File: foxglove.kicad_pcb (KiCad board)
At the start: 4 copper layers, 82.8 x 53.3 mm, 177 parts, among them IC1 LFE5U-12F-6BG256C, J1 NEIGHBOR1, J2 NEIGHBOR2, J3 Conn_02x05_Odd_Even, J4 Conn_02x10_Odd_Even, J5 Conn_01x02_Female, J6 Conn_02x03_Odd_Even, J7 BONUS_ROW, U1 LM393, U10 SHIFTER, U11 74HC4051, U12 SHIFTER, U13 74HC4051, U14 SHIFTER, U15 74HC4051, U16 SHIFTER, U17 74HC4051, U18 SHIFTER, U19 74HC4051, U2 ADP225, U20 SHIFTER, U21 74HC4051, U22 SHIFTER, U23 74HC4051, U24 SHIFTER, U25 74LVC1G53, U26 PCA6408A, U3 AP2127, U4 74LVC1G3157, U5 AP2127, U6 AP2127, U7 DAC084S085, U8 AT25xxx, U9 74HC4051

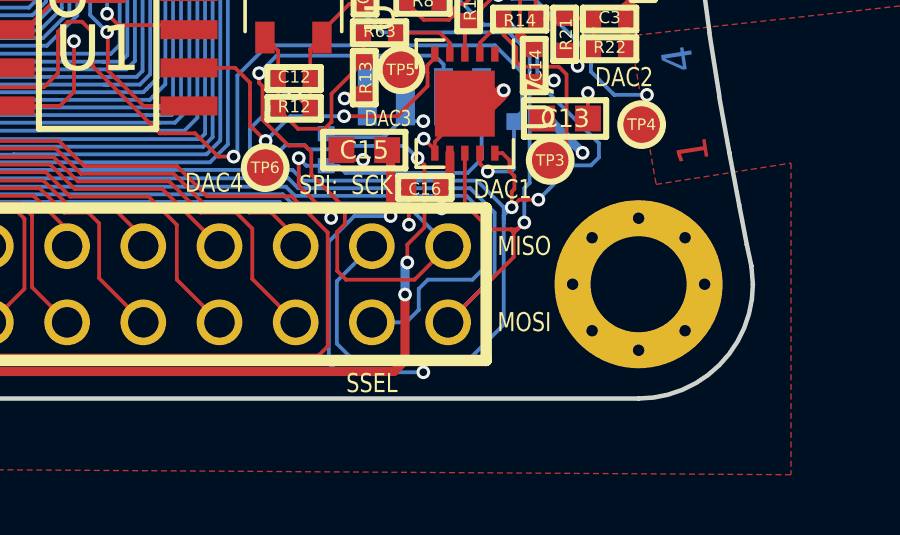
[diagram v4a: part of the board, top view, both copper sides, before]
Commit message: adopt OSHWA convention for SPI signal names https://www.oshwa.org/a-resolution-to-redefine-spi-signal-names
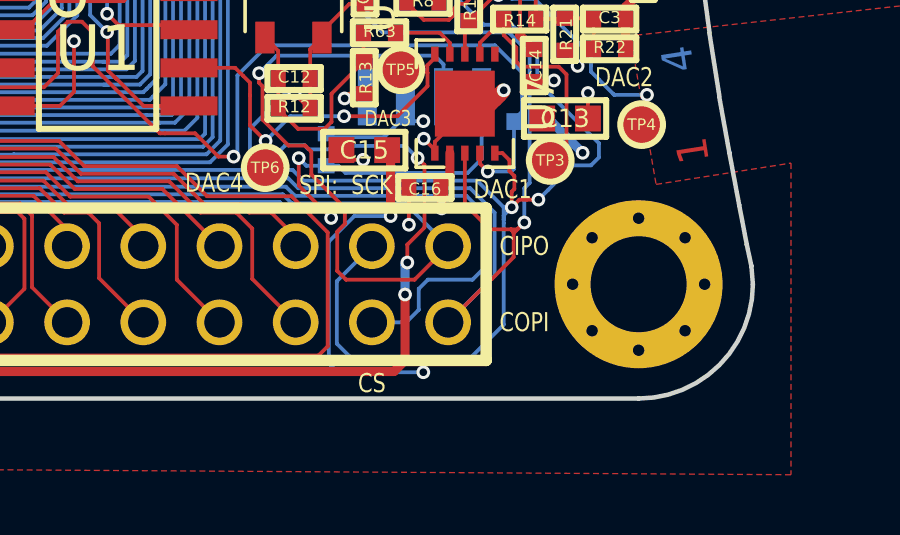
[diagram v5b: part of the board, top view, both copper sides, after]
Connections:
- net /MISO renamed /CIPO
- net /MOSI renamed /COPI
- net /SSEL renamed /CS
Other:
- board text added: "CIPO"
- board text added: "COPI"
- board text added: "CS"
- board text removed: "MISO"
- board text removed: "MOSI"
- board text removed: "SSEL"
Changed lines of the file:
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@@
   (net 18 /J1.35)
   (net 19 /J1.36)
-  (net 20 /SSEL)
+  (net 20 /CS)
   (net 21 /SCK)
-  (net 22 /MOSI)
-  (net 23 /MISO)
+  (net 22 /COPI)
+  (net 23 /CIPO)
   (net 24 /ADC)
   (net 25 /J2.09)
@@
     (add_net /J7.17)
     (add_net /J7.18)
-    (add_net /MISO)
-    (add_net /MOSI)
+    (add_net /CIPO)
+    (add_net /COPI)
     (add_net /PROGRAMN)
     (add_net /S0_1)
@@
     (add_net /S2_8)
     (add_net /SCK)
-    (add_net /SSEL)
+    (add_net /CS)
     (add_net /TCK)
     (add_net /TDI)
@@
       (net 94 /INITN))
     (pad T8 smd circle (at -0.4 6 90) (size 0.41 0.41) (layers F.Cu F.Paste F.Mask)
-      (net 22 /MOSI))
+      (net 22 /COPI))
     (pad T7 smd circle (at -1.2 6 90) (size 0.41 0.41) (layers F.Cu F.Paste F.Mask)
-      (net 23 /MISO))
+      (net 23 /CIPO))
     (pad T6 smd circle (at -2 6 90) (size 0.41 0.41) (layers F.Cu F.Paste F.Mask)
       (net 101 /J1.22))
@@
       (net 91 /PROGRAMN))
     (pad R8 smd circle (at -0.4 5.2 90) (size 0.41 0.41) (layers F.Cu F.Paste F.Mask)
-      (net 20 /SSEL))
+      (net 20 /CS))
     (pad R7 smd circle (at -1.2 5.2 90) (size 0.41 0.41) (layers F.Cu F.Paste F.Mask)
       (net 241 "Net-(IC1-PadR7)"))
@@
     (fp_line (start -25.4 -2.54) (end 25.4 -2.54) (layer F.SilkS) (width 0.381))
     (pad 40 thru_hole circle (at 24.13 -1.27) (size 1.524 1.524) (drill 1.016) (layers *.Cu *.Mask F.SilkS)
-      (net 23 /MISO))
+      (net 23 /CIPO))
     (pad 39 thru_hole circle (at 24.13 1.27) (size 1.524 1.524) (drill 1.016) (layers *.Cu *.Mask F.SilkS)
-      (net 22 /MOSI))
+      (net 22 /COPI))
     (pad 38 thru_hole circle (at 21.59 -1.27) (size 1.524 1.524) (drill 1.016) (layers *.Cu *.Mask F.SilkS)
       (net 21 /SCK))
     (pad 37 thru_hole circle (at 21.59 1.27) (size 1.524 1.524) (drill 1.016) (layers *.Cu *.Mask F.SilkS)
-      (net 20 /SSEL))
+      (net 20 /CS))
     (pad 36 thru_hole circle (at 19.05 -1.27) (size 1.524 1.524) (drill 1.016) (layers *.Cu *.Mask F.SilkS)
       (net 19 /J1.36))
@@
       (net 292 /DAC~SYNC~))
     (pad 8 smd rect (at 1.65 0 270) (size 0.5 0.25) (layers F.Cu F.Paste F.Mask)
-      (net 22 /MOSI))
+      (net 22 /COPI))
     (pad 5 smd rect (at -1.65 1 270) (size 0.5 0.25) (layers F.Cu F.Paste F.Mask)
       (net 65 /DAC4))
@@
       (net 88 /CSSPIN))
     (pad 2 smd rect (at -3.048 0.635 90) (size 1.905 0.635) (layers B.Cu B.Paste B.Mask)
-      (net 23 /MISO))
+      (net 23 /CIPO))
     (pad 3 smd rect (at -3.048 -0.635 90) (size 1.905 0.635) (layers B.Cu B.Paste B.Mask)
       (net 2 VCC))
@@
       (net 1 GND))
     (pad 5 smd rect (at 3.048 -1.905 90) (size 1.905 0.635) (layers B.Cu B.Paste B.Mask)
-      (net 22 /MOSI))
+      (net 22 /COPI))
     (pad 6 smd rect (at 3.048 -0.635 90) (size 1.905 0.635) (layers B.Cu B.Paste B.Mask)
       (net 21 /SCK))
@@
     (effects (font (size 0.635 0.508) (thickness 0.1016)))
   )
-  (gr_text SSEL (at 167.64 121.412) (layer F.SilkS)
+  (gr_text CS (at 167.64 121.412) (layer F.SilkS)
     (effects (font (size 0.635 0.508) (thickness 0.1016)))
   )
-  (gr_text MISO (at 172.72 116.84) (layer F.SilkS)
+  (gr_text CIPO (at 172.72 116.84) (layer F.SilkS)
     (effects (font (size 0.635 0.508) (thickness 0.1016)))
   )
-  (gr_text MOSI (at 172.72 119.38) (layer F.SilkS)
+  (gr_text COPI (at 172.72 119.38) (layer F.SilkS)
     (effects (font (size 0.635 0.508) (thickness 0.1016)))
   )
